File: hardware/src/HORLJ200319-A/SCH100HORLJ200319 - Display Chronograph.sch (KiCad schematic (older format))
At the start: 50 parts

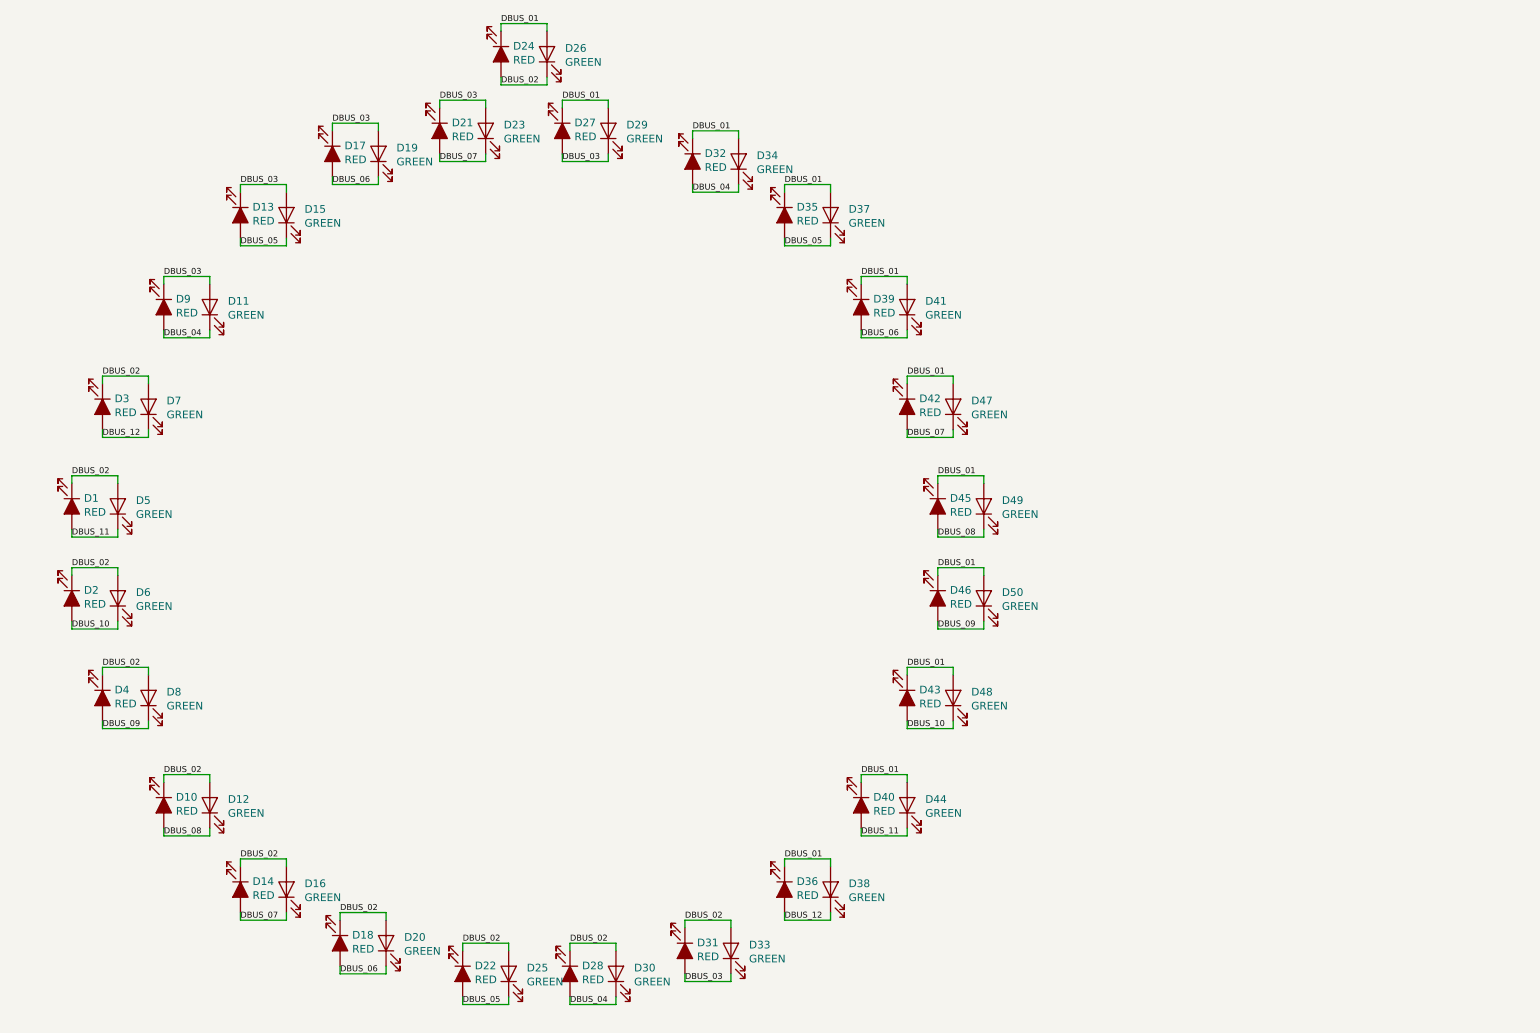
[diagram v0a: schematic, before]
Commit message: Insere MockUps digitais e inicia o projeto da PCB.
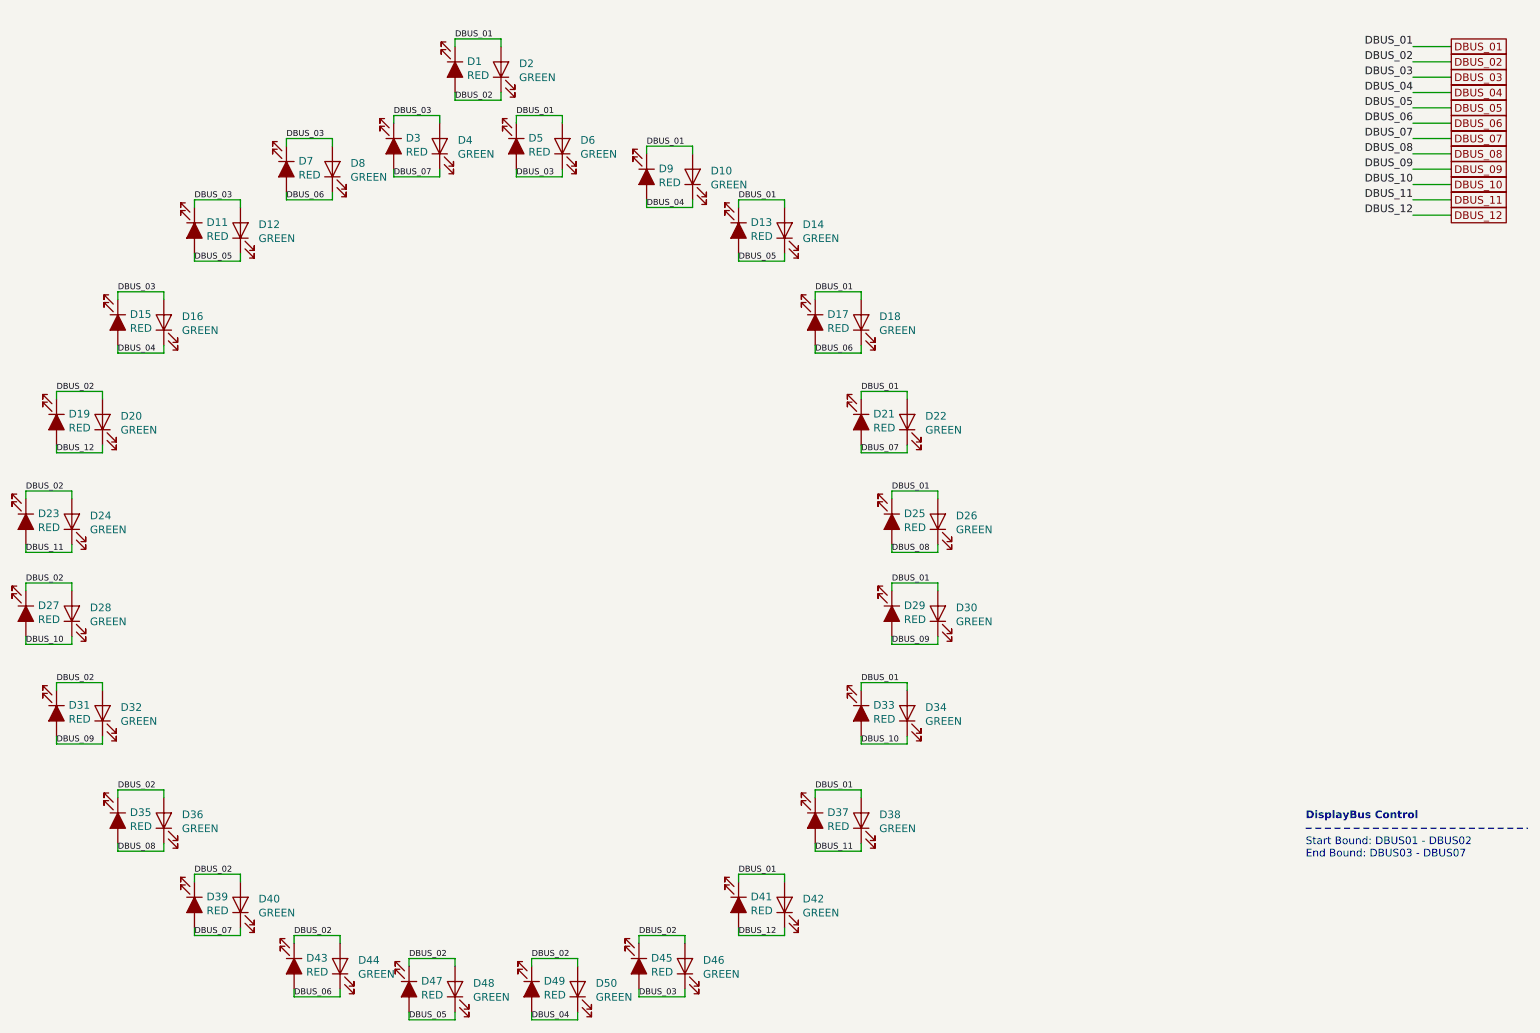
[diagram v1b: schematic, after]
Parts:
- renumbered D24 to D1, D34 to D10, D13 to D11, D15 to D12, D35 to D13, D37 to D14, D9 to D15, D11 to D16, D39 to D17, D41 to D18, D3 to D19, D26 to D2, D7 to D20, D42 to D21, D47 to D22, D1 to D23, D5 to D24, D45 to D25, D49 to D26, D2 to D27, D6 to D28, D46 to D29, D21 to D3, D50 to D30, D4 to D31, D8 to D32, D43 to D33, D48 to D34, D10 to D35, D12 to D36, D40 to D37, D44 to D38, D14 to D39, D23 to D4, D16 to D40, D36 to D41, D38 to D42, D18 to D43, D20 to D44, D31 to D45, D33 to D46, D22 to D47, D25 to D48, D28 to D49, D27 to D5, D30 to D50, D29 to D6, D17 to D7, D19 to D8, D32 to D9
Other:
- note added: "DisplayBus Control"
- note added: "Start Bound: DBUS01 - DBUS02\nEnd Bound: DBUS03 - DBUS07"
- moved on the sheet: D1, D10, D11, D12, D13, D14, D15, D16, D17, D18, D19, D2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
